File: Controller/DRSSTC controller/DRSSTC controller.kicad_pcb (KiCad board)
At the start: 2 copper layers, 110.5 x 47 mm, 108 parts, among them J1 Conn_01x01_Female, J2 Screw_Terminal_01x02, J3 Conn_01x01_Female, J4 Conn_01x01_Female, J401 Conn_01x01_Female, J402 Screw_Terminal_01x02, J403 Conn_01x01_Female, J5 Screw_Terminal_01x02, J507 Conn_01x03_Male, J508 Conn_01x02_Male, J509 Conn_01x02_Male, J510 Conn_01x02_Male, J6 Conn_01x01_Female, J7 Conn_01x01_Female, J8 Screw_Terminal_01x02, J9 Conn_01x01_Female, Q401 Q_PMOS_GDS, Q402 Q_NMOS_GDS, Q403 Q_PMOS_GDS, Q404 Q_NMOS_GDS, U401 UCC27524, U501 Optical_reciver, U502 Optical_reciver, U503 74HC14, U504 LM311, U505 74HC74, U506 74LS00, U507 TLV7031DBV, U601 L7809, U602 L7805

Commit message: V0.15a
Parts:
- added C3: 100n, Capacitor_SMD:C_0805_2012Metric, F.Cu at (115.3, 90.7)
- added C4: 100n, Capacitor_SMD:C_0805_2012Metric, F.Cu at (114.6, 102.6)
- added C5: 470u, Capacitor_THT:CP_Radial_D5.0mm_P2.50mm, F.Cu at (118.9, 101.4)
- added H1: MountingHole, MountingHole:MountingHole_3.2mm_M3, F.Cu at (50.0, 86.1)
- added H2: MountingHole, MountingHole:MountingHole_3.2mm_M3, F.Cu at (122.4, 86.1)
- added H3: MountingHole, MountingHole:MountingHole_3.2mm_M3, F.Cu at (50.0, 158.5)
- added H4: MountingHole, MountingHole:MountingHole_3.2mm_M3, F.Cu at (122.4, 158.2)
- added J10: Conn_01x02_Male, Connector_PinHeader_2.54mm:PinHeader_1x02_P2.54mm_Vertical, F.Cu at (124.0, 103.9)
- added U1: L7812, Package_TO_SOT_SMD:TO-252-2, F.Cu at (118.6, 95.5)
- C602: footprint Capacitor_THT:CP_Radial_D5.0mm_P2.50mm -> Capacitor_THT:C_Radial_D12.5mm_H25.0mm_P5.00mm
- Q401, Q402, Q403, Q404: footprint Package_TO_SOT_SMD:TO-252-3_TabPin2 -> Package_TO_SOT_SMD:TO-252-2
- moved U501 108.0 mm to (64.5, 155.2)
- moved R501 106.6 mm to (62.7, 149.6), turned to 180 degrees
- moved C503 96.9 mm to (50.3, 121.9), turned to 0 degrees
- moved C504 96.5 mm to (72.6, 121.7), turned to 90 degrees
- moved C405 86.4 mm to (98.8, 135.4), turned to -90 degrees
- moved C402 85.8 mm to (102.4, 141.0)
- moved C401 85.5 mm to (102.4, 157.2)
- moved Q404 84.8 mm to (110.6, 138.7)
- moved C1 84.7 mm to (91.9, 148.6), turned to 180 degrees
- moved U502 84.5 mm to (77.0, 155.2)
- moved Q402 84.3 mm to (110.6, 154.9)
- moved C2 84.1 mm to (98.0, 145.3), turned to 180 degrees
- moved C506 82.3 mm to (59.7, 148.6), turned to -90 degrees
- moved U401 82.2 mm to (91.9, 144.3)
- moved D1 81.7 mm to (101.1, 147.2)
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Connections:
- net Net-(C405-Pad1) renamed /GDT_primary/BottomSide_PGate
- net Net-(C405-Pad2) renamed /GDT_primary/BottomSide_NGate
- net Net-(C406-Pad2) renamed /GDT_primary/GDT_terminal_B
- net Net-(D601-Pad2) renamed /Power_regulation/Vcc_LED
- net Net-(D602-Pad2) renamed /Power_regulation/9V_LED
- net Net-(D603-Pad2) renamed /Power_regulation/5V_LED
- net Net-(J402-Pad2) renamed /GDT_primary/GDT_terminal_A
- net Net-(Q401-Pad1) renamed /GDT_primary/TopSide_PGate
- net Net-(Q402-Pad1) renamed /GDT_primary/TopSide_NGate
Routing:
- net LED_overcurrent: track 25.5 -> 56.1 mm
- net +5V: track 0.00 -> 30.3 mm, vias 0 -> 2
- net LED_inteep: track 47.2 -> 67.1 mm, vias 2 -> 3
- net /GDT_primary/GDT_terminal_B: track 15.9 -> 0.00 mm
- net Net-(C509-Pad1): track 34.5 -> 19.3 mm
- net Net-(R501-Pad2): track 36.4 -> 21.4 mm, vias 1 -> 0
- net Net-(U505-Pad9): track 37.8 -> 23.1 mm, vias 2 -> 3
- net +9V: track 0.00 -> 14.5 mm, vias 0 -> 2
- net Net-(U503-Pad10): track 26.3 -> 11.9 mm
- net +12V: track 0.00 -> 13.5 mm
- net Net-(C406-Pad1): track 12.6 -> 0.00 mm
- net /GDT_primary/GDT_terminal_A: track 12.6 -> 0.00 mm
- net Net-(C514-Pad2): track 45.8 -> 35.7 mm, vias 2 -> 0
- net Net-(U505-Pad5): track 27.5 -> 17.8 mm, vias 2 -> 0
- net GND: track 100.3 -> 107.9 mm, vias 74 -> 84
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- added copper zone on F.Cu, net /GDT_primary/GDT_terminal_B
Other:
- board size 110.5 x 47 mm -> 80 x 80 mm

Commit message: v0.15b
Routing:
- net Net-(C514-Pad2): track 35.7 -> 63.9 mm, vias 0 -> 2
- net LED_overcurrent: track 56.1 -> 57.5 mm
- net Net-(U505-Pad5): track 17.8 -> 18.6 mm
- net LED_inteep: vias 3 -> 5

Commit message: V0.2a
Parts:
- added kibuzzard-64072E65: G***, kibuzzard-64072E65, F.Cu at (121.9, 124.7)
- added kibuzzard-64072E6F: G***, kibuzzard-64072E6F, F.Cu at (106.9, 91.2)
- added kibuzzard-64072E85: G***, kibuzzard-64072E85, F.Cu at (58.9, 94.7)
- added kibuzzard-64072E9F: G***, kibuzzard-64072E9F, F.Cu at (61.5, 125.5)
- added kibuzzard-64072EC9: G***, kibuzzard-64072EC9, F.Cu at (88.9, 159.8)

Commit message: V0.2c
Added stl files
PCB update
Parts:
- C403: renamed from C602; footprint Capacitor_THT:C_Radial_D12.5mm_H25.0mm_P5.00mm -> Capacitor_THT:CP_Radial_D12.5mm_P5.00mm
- moved RV301 0.51 mm to (52.6, 143.7)
- moved C403 0.39 mm to (97.3, 89.4)
- renumbered C401 to C201, C402 to C202, C1 to C203, C2 to C204, C405 to C205, C406 to C206, C407 to C207, C501 to C301, C502 to C302, C503 to C303, C504 to C304, C505 to C305, C506 to C306, C507 to C307, C508 to C308, C509 to C309, C510 to C310, C511 to C311, C512 to C312, C513 to C313, C514 to C314, C515 to C315, C3 to C401, C601 to C402, C4 to C404, C5 to C405, C603 to C406, C604 to C407, C605 to C408, C606 to C409, C607 to C410, D1 to D201, D2 to D202, D501 to D301, D502 to D302, D503 to D303, D504 to D304, D505 to D305, D506 to D306, D507 to D307, D508 to D308, D509 to D309, D510 to D310, D511 to D311, D601 to D401, D602 to D402, D603 to D403, J401 to J201, J402 to J202, J403 to J203, J1 to J301, J2 to J302, J3 to J303, J4 to J304, J5 to J305, J6 to J306, J507 to J307, J508 to J308, J509 to J309, J510 to J310, J7 to J401, J8 to J402, J9 to J403, J10 to J404, L501 to L301, Q401 to Q201, Q402 to Q202, Q403 to Q203, Q404 to Q204, R401 to R201, R402 to R202, R403 to R203, R501 to R301, R502 to R302, R503 to R303, R504 to R304, R505 to R305, R506 to R306, R507 to R307, R508 to R308, R509 to R309, R510 to R310, R511 to R311, R512 to R312, R513 to R313, R514 to R314, R515 to R315, R516 to R316, R517 to R317, R518 to R318, R519 to R319, R601 to R401, R602 to R402, R603 to R403, RV501 to RV301, TP501 to TP301, TP502 to TP302, TP503 to TP303, TP504 to TP304, TP505 to TP305, TP506 to TP306, U401 to U201, U501 to U301, U502 to U302, U503 to U303, U504 to U304, U505 to U305, U506 to U306, U507 to U307, U1 to U401, U601 to U402, U602 to U403
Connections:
- net /GDT_primary/BottomSide_NGate renamed Net-(C205-Pad2)
- net /GDT_primary/BottomSide_PGate renamed Net-(C205-Pad1)
- net /GDT_primary/GDT_terminal_A renamed Net-(J202-Pad2)
- net /GDT_primary/GDT_terminal_B renamed Net-(C206-Pad2)
- net /GDT_primary/TopSide_NGate renamed Net-(C204-Pad2)
- net /GDT_primary/TopSide_PGate renamed Net-(C204-Pad1)
- net /Power_regulation/5V_LED renamed Net-(D403-Pad2)
- net /Power_regulation/9V_LED renamed Net-(D402-Pad2)
- net /Power_regulation/Vcc_LED renamed Net-(D401-Pad2)

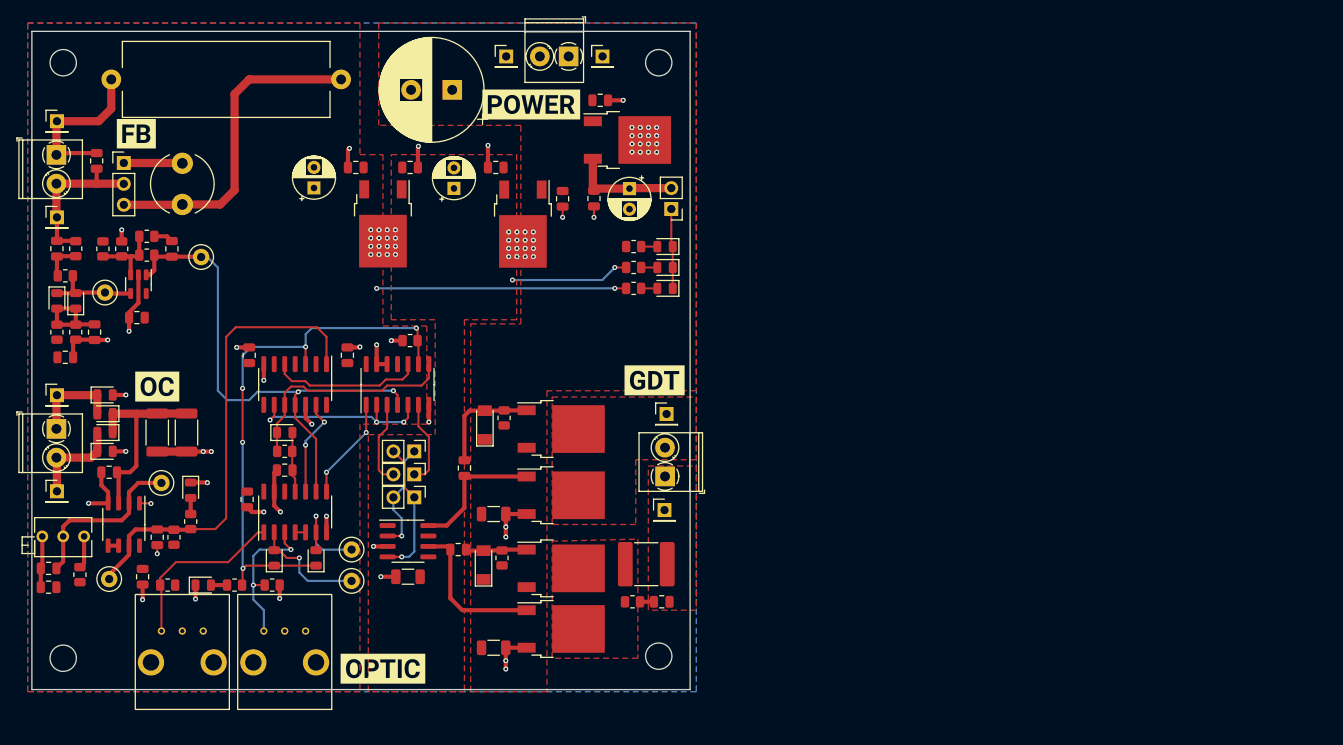
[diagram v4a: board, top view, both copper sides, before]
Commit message: Updated circuit
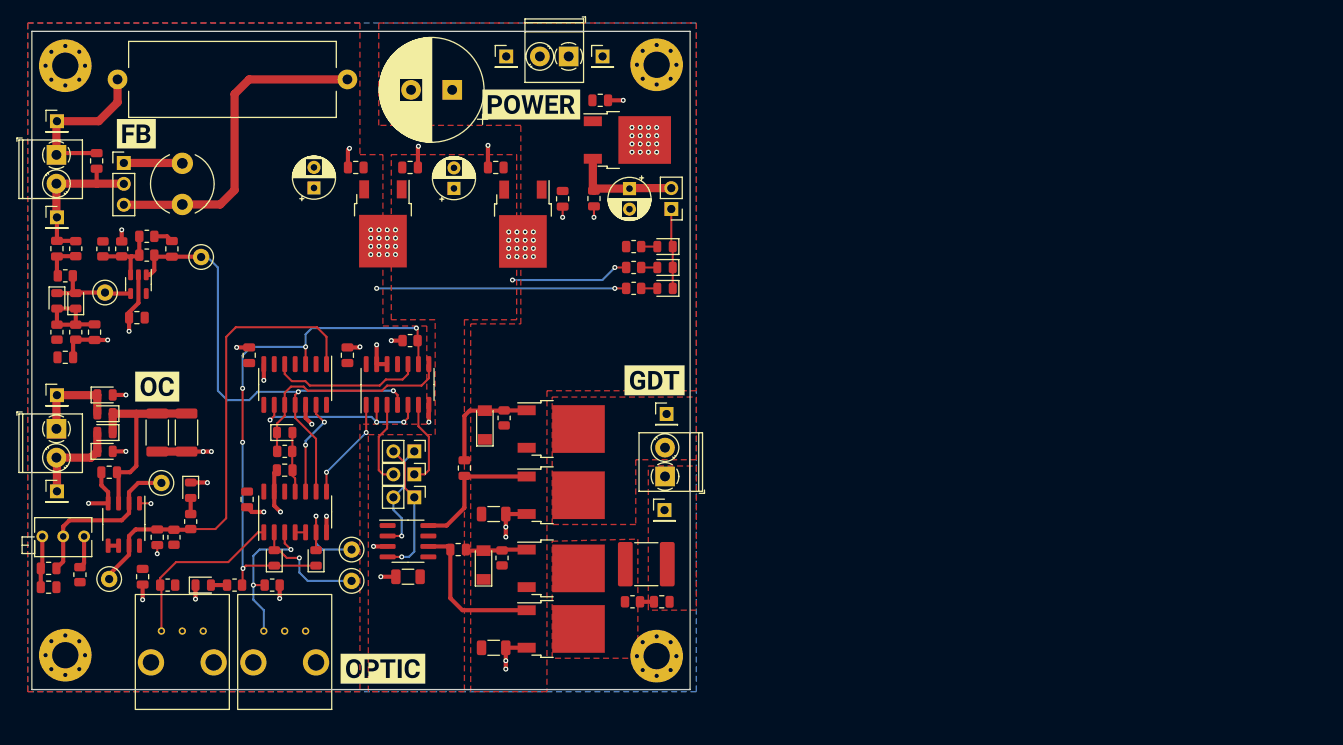
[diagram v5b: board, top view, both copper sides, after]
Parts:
- removed H1, H2, H3, H4: MountingHole, MountingHole:MountingHole_3.2mm_M3
- added H201: MountingHole_Pad, MountingHole:MountingHole_3.2mm_M3_Pad_Via, F.Cu at (122.2, 86.4)
- added H202: MountingHole_Pad, MountingHole:MountingHole_3.2mm_M3_Pad_Via, F.Cu at (50.3, 86.5)
- added H203: MountingHole_Pad, MountingHole:MountingHole_3.2mm_M3_Pad_Via, F.Cu at (50.3, 158.1)
- added H204: MountingHole_Pad, MountingHole:MountingHole_3.2mm_M3_Pad_Via, F.Cu at (122.2, 158.2)
- added kibuzzard-6412189F: G***, kibuzzard-6412189F, B.Cu at (109.7, 149.6)
- added kibuzzard-64121B21: G***, kibuzzard-64121B21, B.Cu at (77.5, 116.1)
- moved R305 0.76 mm to (84.6, 88.1)
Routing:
- net Net-(J307-Pin_3): track 39.6 -> 40.3 mm
